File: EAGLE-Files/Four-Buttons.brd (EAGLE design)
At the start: 49.5 x 31.8 mm, 8 parts

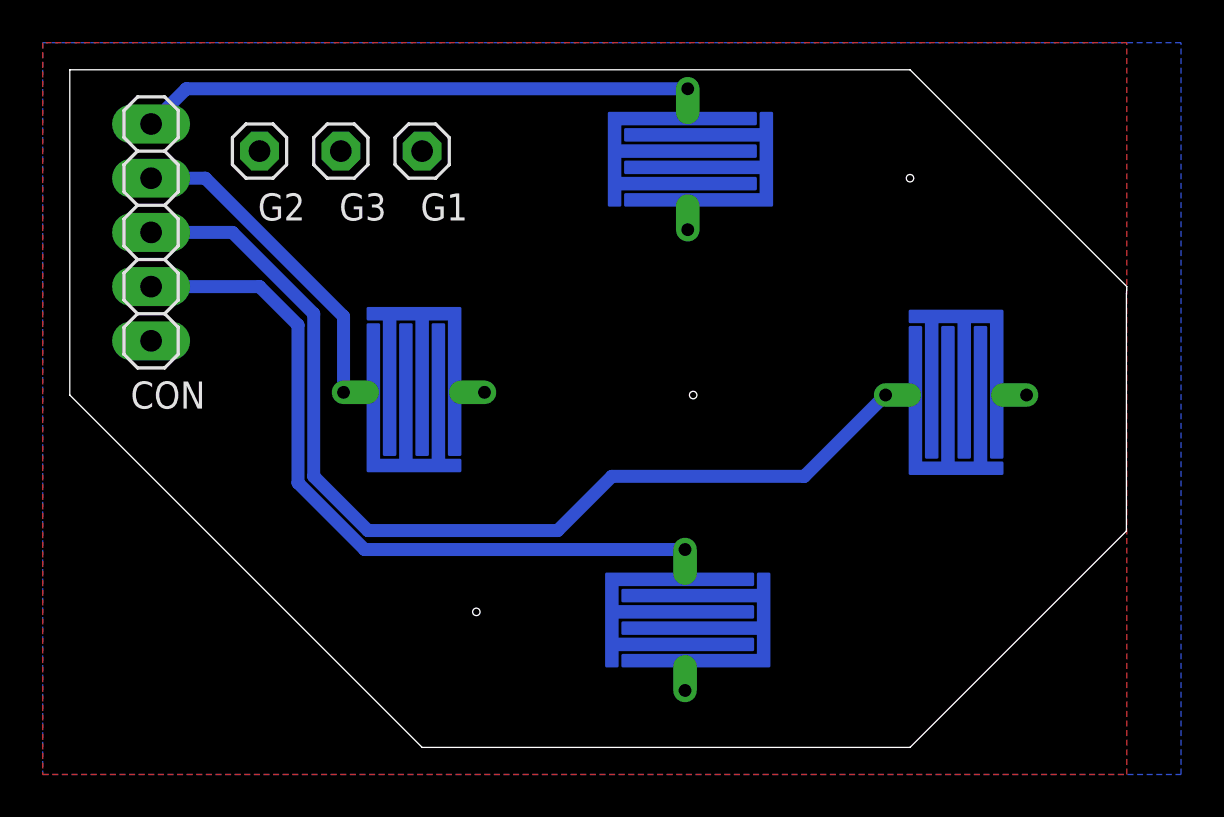
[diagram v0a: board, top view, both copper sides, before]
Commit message: Updated the DPad and Four Buttons PCB designs for production
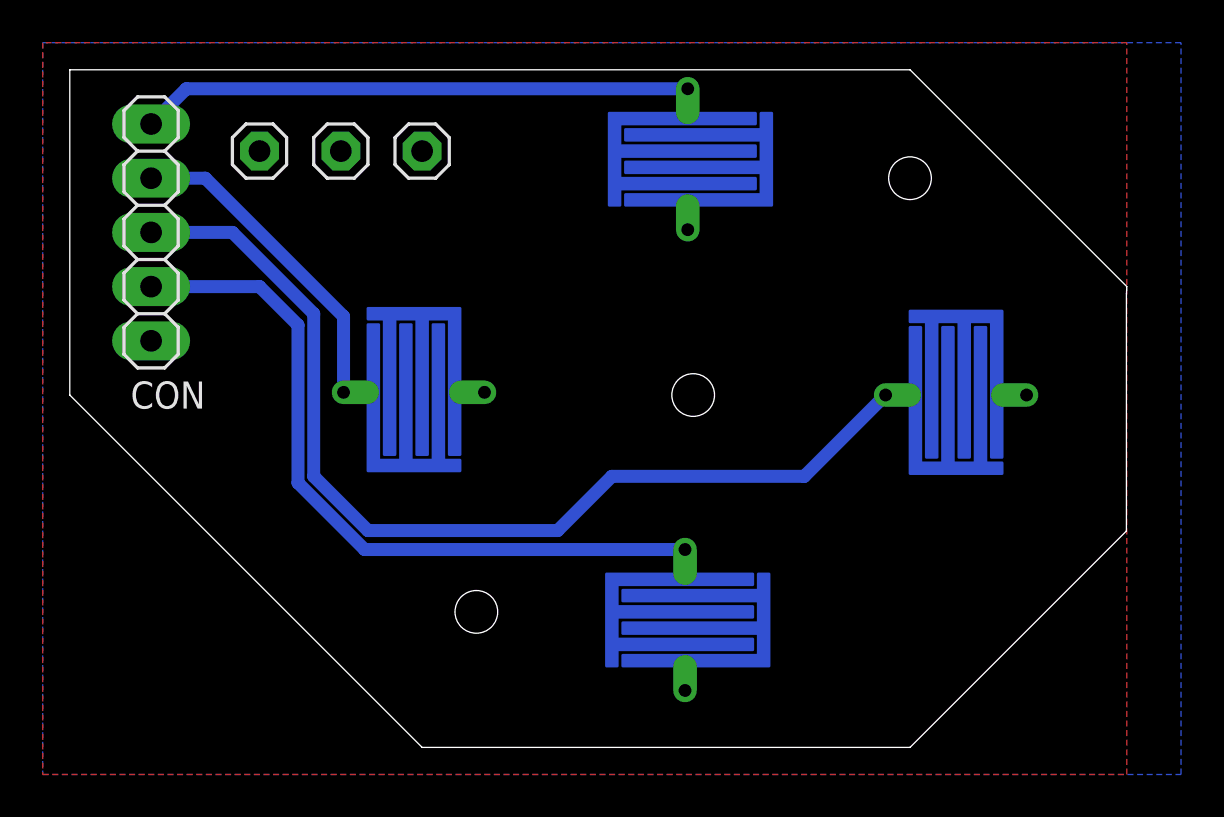
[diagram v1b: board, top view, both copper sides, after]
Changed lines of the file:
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@@
 <wire x1="39.37" y1="31.75" x2="0" y2="31.75" width="0" layer="20"/>
 <wire x1="0" y1="31.75" x2="0" y2="16.51" width="0" layer="20"/>
-<dimension x1="0" y1="34.29" x2="49.53" y2="34.29" x3="24.765" y3="39.37" textsize="1.778" layer="1"/>
-<dimension x1="52.07" y1="34.29" x2="52.07" y2="0" x3="58.42" y3="17.145" textsize="1.778" layer="1"/>
-<hole x="19.05" y="6.35" drill="0.35"/>
-<hole x="39.37" y="26.67" drill="0.35"/>
-<hole x="29.21" y="16.51" drill="0.35"/>
+<hole x="19.05" y="6.35" drill="2"/>
+<hole x="39.37" y="26.67" drill="2"/>
+<hole x="29.21" y="16.51" drill="2"/>
 </plain>
 <attributes>
@@
 </element>
 <element name="G1" library="pinhead" library_urn="urn:adsk.eagle:library:325" package="1X01" package3d_urn="urn:adsk.eagle:package:22485/2" value="" x="16.51" y="27.94" smashed="yes">
-<attribute name="NAME" x="16.4338" y="24.6888" size="1.27" layer="25" ratio="10"/>
 <attribute name="POPULARITY" value="64" x="16.51" y="27.94" size="1.778" layer="27" display="off"/>
 <attribute name="VALUE" x="15.24" y="24.765" size="1.27" layer="27"/>
 </element>
 <element name="G2" library="pinhead" library_urn="urn:adsk.eagle:library:325" package="1X01" package3d_urn="urn:adsk.eagle:package:22485/2" value="" x="8.89" y="27.94" smashed="yes">
-<attribute name="NAME" x="8.8138" y="24.6888" size="1.27" layer="25" ratio="10"/>
 <attribute name="POPULARITY" value="64" x="8.89" y="27.94" size="1.778" layer="27" display="off"/>
 <attribute name="VALUE" x="7.62" y="24.765" size="1.27" layer="27"/>
 </element>
 <element name="G3" library="pinhead" library_urn="urn:adsk.eagle:library:325" package="1X01" package3d_urn="urn:adsk.eagle:package:22485/2" value="" x="12.7" y="27.94" smashed="yes">
-<attribute name="NAME" x="12.6238" y="24.6888" size="1.27" layer="25" ratio="10"/>
 <attribute name="POPULARITY" value="64" x="12.7" y="27.94" size="1.778" layer="27" display="off"/>
 <attribute name="VALUE" x="11.43" y="24.765" size="1.27" layer="27"/>
